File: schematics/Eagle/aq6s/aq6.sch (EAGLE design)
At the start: 26 parts

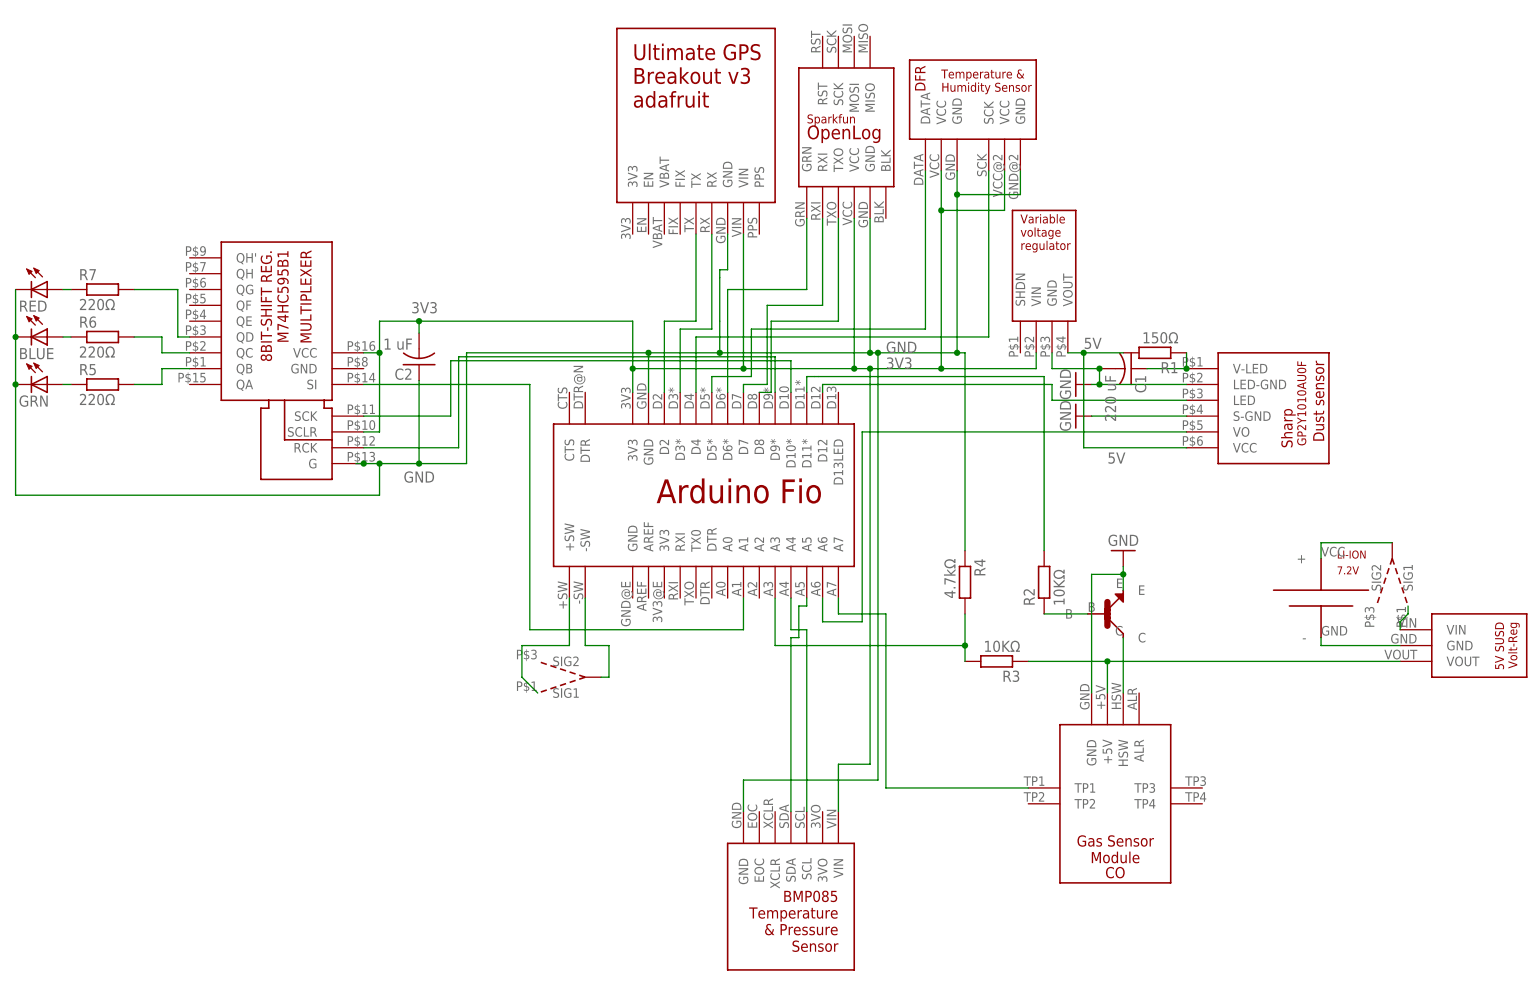
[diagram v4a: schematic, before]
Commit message: Removed mux/bit shift register
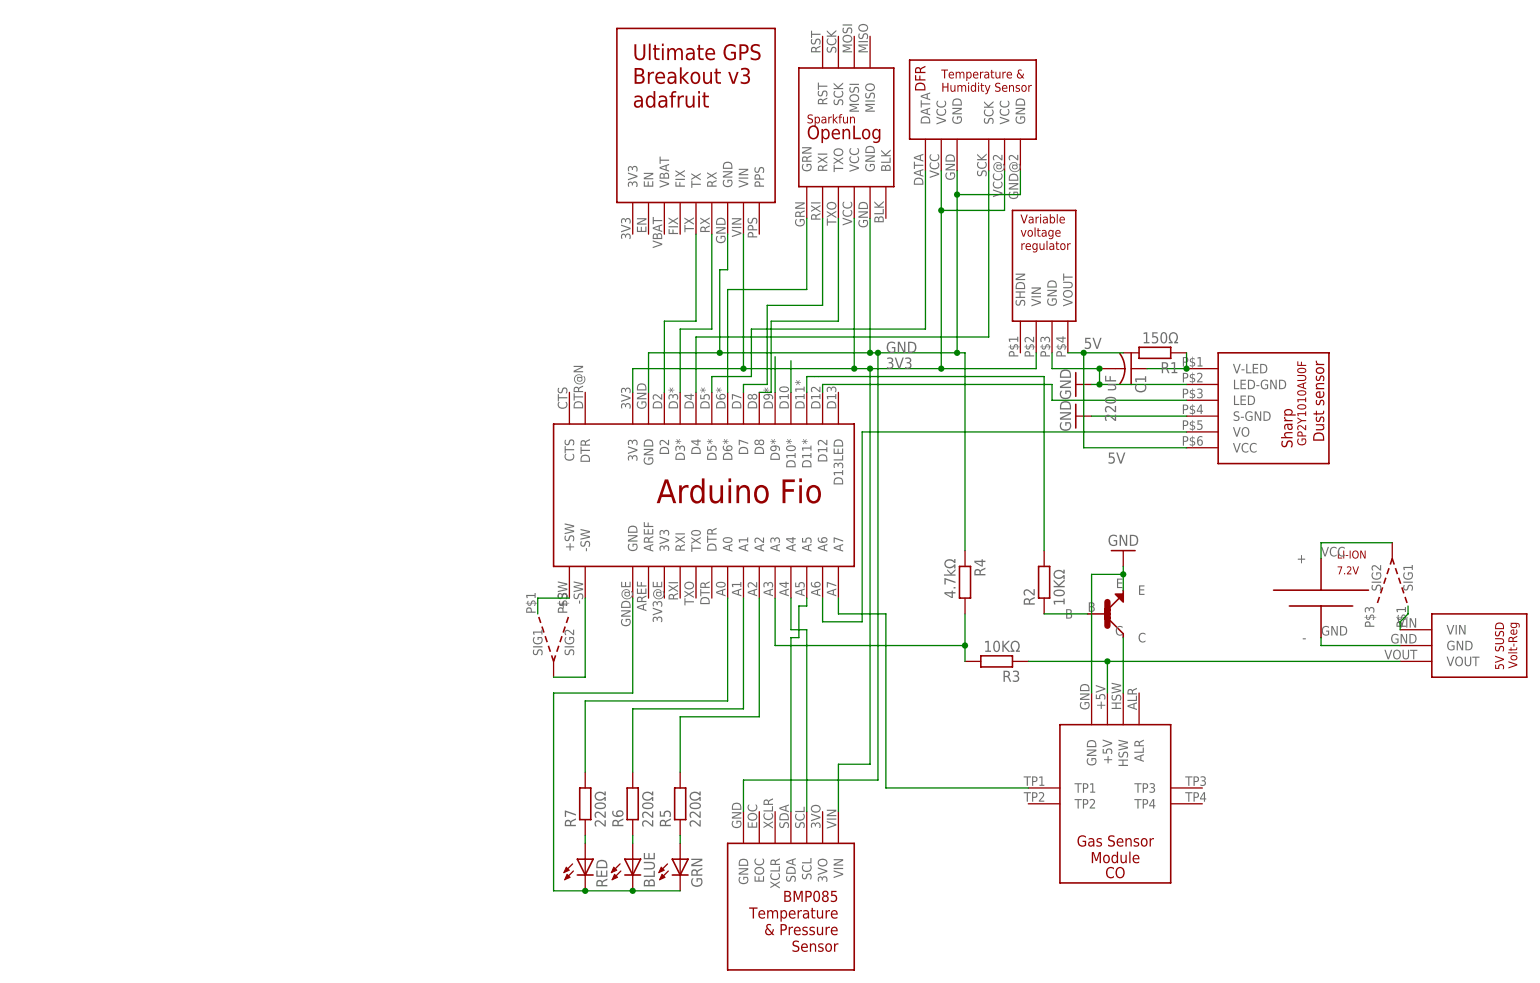
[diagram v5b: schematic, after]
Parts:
- removed C2: 1 uF, resistor:C-US050-025X075
- removed U$9: M74HC595B1, air_quality_parts:M74HC595B1
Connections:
- removed net N$22: U$2.A1, U$9.SI
- removed net N$25: R5.2, U$9.QB
- net 3V3: no longer C2.2, U$9.SCLR, U$9.VCC
- net GND: now also LI-ION.-, U$2.GND@E, U$7.GND; no longer C2.1, U$9.G
- net N$15: now also R5.2, U$2.A2; no longer LI-ION.-, U$7.GND
- net N$26: no longer U$9.SCK
- net N$27: no longer U$9.RCK
- net N$28: now also U$2.A0; no longer U$9.QD
- net N$29: now also U$2.A1; no longer U$9.QC
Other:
- moved on the sheet: BLUE, GRN, R5, R6, R7, RED

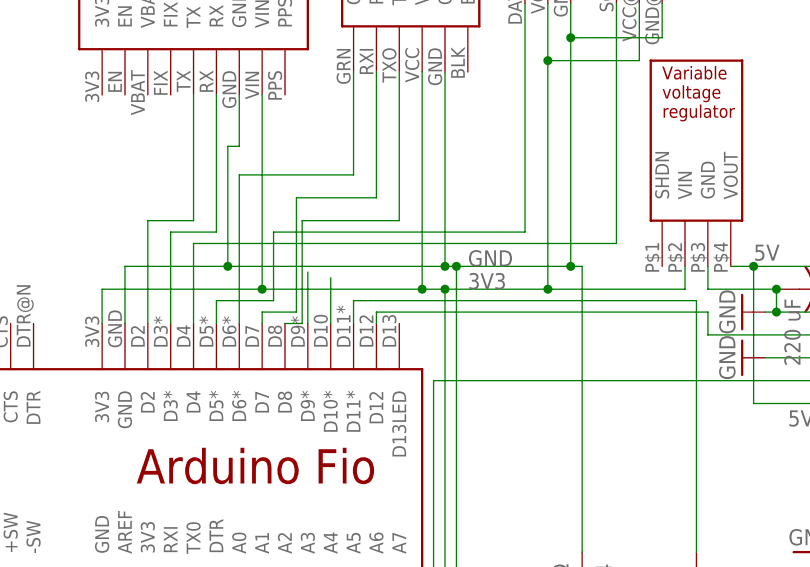
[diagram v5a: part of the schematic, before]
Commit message: Thickened pcd traces
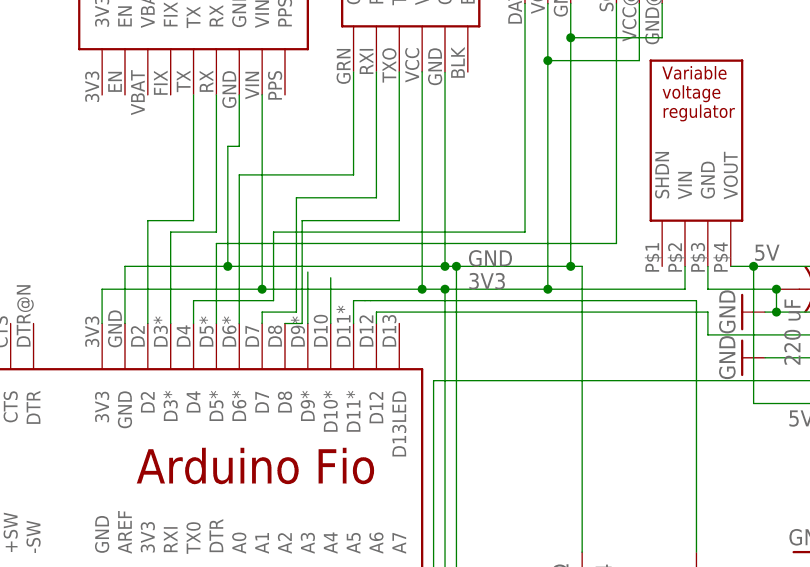
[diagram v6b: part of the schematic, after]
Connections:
- net N$12: now also U$2.D5*; no longer U$2.D4
- net N$13: now also U$2.D4; no longer U$2.D5*
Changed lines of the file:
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@@
 <pinref part="U$6" gate="G$1" pin="SCK"/>
 <wire x1="72.39" y1="87.63" x2="72.39" y2="60.96" width="0.1524" layer="91"/>
-<wire x1="72.39" y1="60.96" x2="25.4" y2="60.96" width="0.1524" layer="91"/>
-<pinref part="U$2" gate="G$1" pin="D4"/>
-<wire x1="25.4" y1="60.96" x2="25.4" y2="52.07" width="0.1524" layer="91"/>
+<wire x1="72.39" y1="60.96" x2="27.94" y2="60.96" width="0.1524" layer="91"/>
+<pinref part="U$2" gate="G$1" pin="D5*"/>
+<wire x1="27.94" y1="60.96" x2="27.94" y2="52.07" width="0.1524" layer="91"/>
 </segment>
 </net>
@@
 <wire x1="62.23" y1="62.23" x2="34.29" y2="62.23" width="0.1524" layer="91"/>
 <wire x1="34.29" y1="62.23" x2="34.29" y2="54.61" width="0.1524" layer="91"/>
-<pinref part="U$2" gate="G$1" pin="D5*"/>
-<wire x1="34.29" y1="54.61" x2="27.94" y2="54.61" width="0.1524" layer="91"/>
-<wire x1="27.94" y1="54.61" x2="27.94" y2="52.07" width="0.1524" layer="91"/>
+<wire x1="34.29" y1="54.61" x2="25.4" y2="54.61" width="0.1524" layer="91"/>
+<pinref part="U$2" gate="G$1" pin="D4"/>
+<wire x1="25.4" y1="54.61" x2="25.4" y2="52.07" width="0.1524" layer="91"/>
 </segment>
 </net>

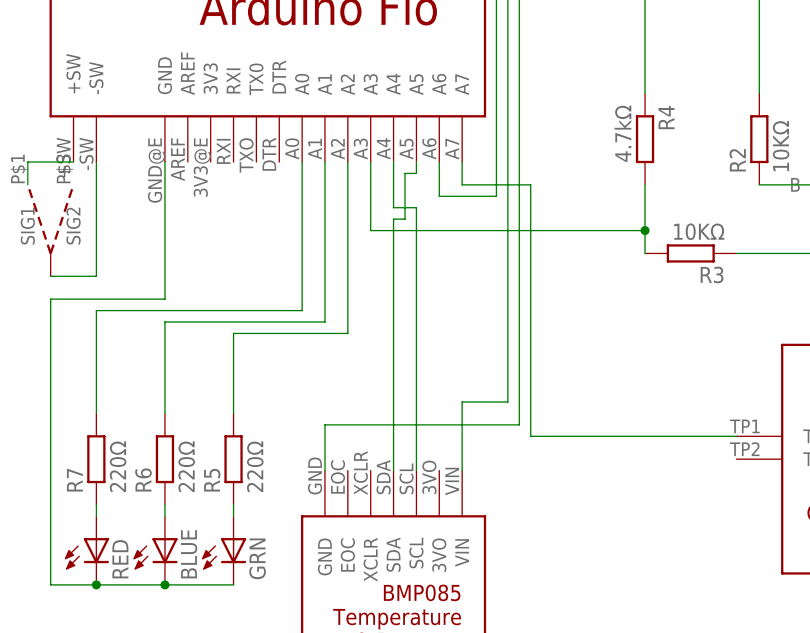
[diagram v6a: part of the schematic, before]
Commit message: Fixed pcb, reexport to png! Update Ard. code
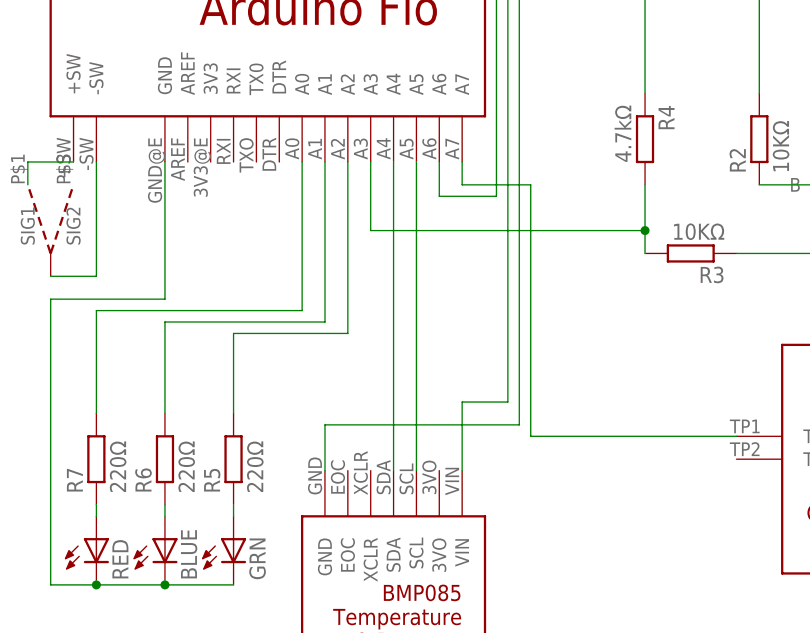
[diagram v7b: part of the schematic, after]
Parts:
- R1: device resistor:R-EU_0204/7 -> rcl:R-EU_0207/15
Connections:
- removed net N$24: U$2.A5, U$8.SDA
- new net N$22: U$2.A4, U$8.SDA
- net N$23: now also U$2.A5; no longer U$2.A4
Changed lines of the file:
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@@
 <part name="GND2" library="supply1" deviceset="GND" device=""/>
 <part name="C1" library="resistor" deviceset="C-US" device="050-025X075" value="220 uF"/>
-<part name="R1" library="resistor" deviceset="R-EU_" device="0204/7" value="150Ω"/>
+<part name="R1" library="rcl" deviceset="R-EU_" device="0207/15" value="150Ω"/>
 <part name="U$3" library="air_quality_parts" deviceset="POLOLU_VAR_VOLTAGE_REG" device=""/>
 <part name="U$4" library="air_quality_parts" deviceset="ADAFRUIT_GPS_V3" device=""/>
@@
 <segment>
 <pinref part="U$8" gate="G$1" pin="SCL"/>
-<wire x1="43.18" y1="-15.24" x2="43.18" y2="13.97" width="0.1524" layer="91"/>
-<pinref part="U$2" gate="G$1" pin="A4"/>
-<wire x1="43.18" y1="13.97" x2="40.64" y2="13.97" width="0.1524" layer="91"/>
-<wire x1="40.64" y1="13.97" x2="40.64" y2="19.05" width="0.1524" layer="91"/>
-</segment>
-</net>
-<net name="N$24" class="0">
-<segment>
-<pinref part="U$8" gate="G$1" pin="SDA"/>
-<wire x1="40.64" y1="-15.24" x2="40.64" y2="12.7" width="0.1524" layer="91"/>
-<wire x1="40.64" y1="12.7" x2="41.91" y2="12.7" width="0.1524" layer="91"/>
-<wire x1="41.91" y1="12.7" x2="41.91" y2="17.78" width="0.1524" layer="91"/>
+<wire x1="43.18" y1="-15.24" x2="43.18" y2="19.05" width="0.1524" layer="91"/>
 <pinref part="U$2" gate="G$1" pin="A5"/>
-<wire x1="41.91" y1="17.78" x2="43.18" y2="17.78" width="0.1524" layer="91"/>
-<wire x1="43.18" y1="17.78" x2="43.18" y2="19.05" width="0.1524" layer="91"/>
 </segment>
 </net>
@@
 </segment>
 </net>
+<net name="N$22" class="0">
+<segment>
+<pinref part="U$8" gate="G$1" pin="SDA"/>
+<pinref part="U$2" gate="G$1" pin="A4"/>
+<wire x1="40.64" y1="-15.24" x2="40.64" y2="19.05" width="0.1524" layer="91"/>
+</segment>
+</net>
